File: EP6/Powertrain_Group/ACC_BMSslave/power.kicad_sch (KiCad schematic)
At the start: 11 parts, among them IC2 LT8631IFE#PBF

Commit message: ACC_BMSslave pcb priliminary layout
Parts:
- R50, R51, R52: footprint Resistor_SMD:R_0603_1608Metric -> Resistor_SMD:R_0402_1005Metric
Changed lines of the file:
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@@
 			)
 		)
-		(property "Footprint" "Resistor_SMD:R_0603_1608Metric"
+		(property "Footprint" "Resistor_SMD:R_0402_1005Metric"
 			(at 41.402 57.15 90)
 			(effects
@@
 			)
 		)
-		(property "Footprint" "Resistor_SMD:R_0603_1608Metric"
+		(property "Footprint" "Resistor_SMD:R_0402_1005Metric"
 			(at 116.332 54.61 90)
 			(effects
@@
 			)
 		)
-		(property "Footprint" "Resistor_SMD:R_0603_1608Metric"
+		(property "Footprint" "Resistor_SMD:R_0402_1005Metric"
 			(at 116.332 62.23 90)
 			(effects

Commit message: [BMSslave] snapshot
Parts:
- C15: renamed from C19; value 0.1u -> 100n
- renumbered C17 to C13, C18 to C14, C20 to C16, C21 to C17, C22 to C18, R50 to R20, R51 to R21, R52 to R22
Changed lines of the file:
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@@
 		(shape input)
 		(at 58.42 35.56 180)
-		(fields_autoplaced yes)
 		(effects
 			(font
@@
 		(shape input)
 		(at 40.64 30.48 180)
-		(fields_autoplaced yes)
 		(effects
 			(font
@@
 		(shape output)
 		(at 152.4 50.8 0)
-		(fields_autoplaced yes)
 		(effects
 			(font
@@
 		(dnp no)
 		(fields_autoplaced yes)
-		(property "Reference" "C21"
+		(property "Reference" "C17"
 			(at 138.43 41.91 0)
 			(effects
@@
 			(project "BMS_Slave_V1(ADBMS1818)"
 				(path "/0942010f-46b1-4fe9-9f5e-a3ebd22b3e41/46164ab6-bc7a-458b-aa2e-57ce2cac15f0"
-					(reference "C21")
+					(reference "C17")
 					(unit 1)
 				)
@@
 		(dnp no)
 		(fields_autoplaced yes)
-		(property "Reference" "#PWR059"
+		(property "Reference" "#PWR031"
 			(at 80.01 80.01 0)
 			(effects
@@
 			(project "BMS_Slave_V1(ADBMS1818)"
 				(path "/0942010f-46b1-4fe9-9f5e-a3ebd22b3e41/46164ab6-bc7a-458b-aa2e-57ce2cac15f0"
-					(reference "#PWR059")
+					(reference "#PWR031")
 					(unit 1)
 				)
@@
 		(dnp no)
 		(fields_autoplaced yes)
-		(property "Reference" "C17"
+		(property "Reference" "C13"
 			(at 46.99 33.02 0)
 			(effects
@@
 			(project "BMS_Slave_V1(ADBMS1818)"
 				(path "/0942010f-46b1-4fe9-9f5e-a3ebd22b3e41/46164ab6-bc7a-458b-aa2e-57ce2cac15f0"
-					(reference "C17")
+					(reference "C13")
 					(unit 1)
 				)
@@
 		(dnp no)
 		(fields_autoplaced yes)
-		(property "Reference" "#PWR062"
+		(property "Reference" "#PWR034"
 			(at 134.62 64.77 0)
 			(effects
@@
 			(project "BMS_Slave_V1(ADBMS1818)"
 				(path "/0942010f-46b1-4fe9-9f5e-a3ebd22b3e41/46164ab6-bc7a-458b-aa2e-57ce2cac15f0"
-					(reference "#PWR062")
+					(reference "#PWR034")
 					(unit 1)
 				)
@@
 		(dnp no)
 		(fields_autoplaced yes)
-		(property "Reference" "C18"
+		(property "Reference" "C14"
 			(at 57.15 55.88 0)
 			(effects
@@
 			(project "BMS_Slave_V1(ADBMS1818)"
 				(path "/0942010f-46b1-4fe9-9f5e-a3ebd22b3e41/46164ab6-bc7a-458b-aa2e-57ce2cac15f0"
-					(reference "C18")
+					(reference "C14")
 					(unit 1)
 				)
@@
 		(dnp no)
 		(fields_autoplaced yes)
-		(property "Reference" "R50"
+		(property "Reference" "R20"
 			(at 45.72 55.88 0)
 			(effects
@@
 			(project "BMS_Slave_V1(ADBMS1818)"
 				(path "/0942010f-46b1-4fe9-9f5e-a3ebd22b3e41/46164ab6-bc7a-458b-aa2e-57ce2cac15f0"
-					(reference "R50")
+					(reference "R20")
 					(unit 1)
 				)
@@
 		(dnp no)
 		(fields_autoplaced yes)
-		(property "Reference" "R51"
+		(property "Reference" "R21"
 			(at 120.65 53.34 0)
 			(effects
@@
 			(project "BMS_Slave_V1(ADBMS1818)"
 				(path "/0942010f-46b1-4fe9-9f5e-a3ebd22b3e41/46164ab6-bc7a-458b-aa2e-57ce2cac15f0"
-					(reference "R51")
+					(reference "R21")
 					(unit 1)
 				)
@@
 		(dnp no)
 		(fields_autoplaced yes)
-		(property "Reference" "#PWR060"
+		(property "Reference" "#PWR032"
 			(at 118.11 72.39 0)
 			(effects
@@
 			(project "BMS_Slave_V1(ADBMS1818)"
 				(path "/0942010f-46b1-4fe9-9f5e-a3ebd22b3e41/46164ab6-bc7a-458b-aa2e-57ce2cac15f0"
-					(reference "#PWR060")
+					(reference "#PWR032")
 					(unit 1)
 				)
@@
 		(dnp no)
 		(fields_autoplaced yes)
-		(property "Reference" "C22"
+		(property "Reference" "C18"
 			(at 138.43 53.34 0)
 			(effects
@@
 			(project "BMS_Slave_V1(ADBMS1818)"
 				(path "/0942010f-46b1-4fe9-9f5e-a3ebd22b3e41/46164ab6-bc7a-458b-aa2e-57ce2cac15f0"
-					(reference "C22")
+					(reference "C18")
 					(unit 1)
 				)
@@
 		(dnp no)
 		(fields_autoplaced yes)
-		(property "Reference" "#PWR058"
+		(property "Reference" "#PWR030"
 			(at 43.18 44.45 0)
 			(effects
@@
 			(project "BMS_Slave_V1(ADBMS1818)"
 				(path "/0942010f-46b1-4fe9-9f5e-a3ebd22b3e41/46164ab6-bc7a-458b-aa2e-57ce2cac15f0"
-					(reference "#PWR058")
+					(reference "#PWR030")
 					(unit 1)
 				)
@@
 		(dnp no)
 		(fields_autoplaced yes)
-		(property "Reference" "C19"
+		(property "Reference" "C15"
 			(at 104.14 27.94 90)
 			(effects
@@
 			)
 		)
-		(property "Value" "0.1u"
+		(property "Value" "100n"
 			(at 104.14 30.48 90)
 			(effects
@@
 			(project "BMS_Slave_V1(ADBMS1818)"
 				(path "/0942010f-46b1-4fe9-9f5e-a3ebd22b3e41/46164ab6-bc7a-458b-aa2e-57ce2cac15f0"
-					(reference "C19")
+					(reference "C15")
 					(unit 1)
 				)
@@
 		(dnp no)
 		(fields_autoplaced yes)
-		(property "Reference" "#PWR061"
+		(property "Reference" "#PWR033"
 			(at 134.62 53.34 0)
 			(effects
@@
 			(project "BMS_Slave_V1(ADBMS1818)"
 				(path "/0942010f-46b1-4fe9-9f5e-a3ebd22b3e41/46164ab6-bc7a-458b-aa2e-57ce2cac15f0"
-					(reference "#PWR061")
+					(reference "#PWR033")
 					(unit 1)
 				)
@@
 		(dnp no)
 		(fields_autoplaced yes)
-		(property "Reference" "R52"
+		(property "Reference" "R22"
 			(at 120.65 60.96 0)
 			(effects
@@
 			(project "BMS_Slave_V1(ADBMS1818)"
 				(path "/0942010f-46b1-4fe9-9f5e-a3ebd22b3e41/46164ab6-bc7a-458b-aa2e-57ce2cac15f0"
-					(reference "R52")
+					(reference "R22")
 					(unit 1)
 				)
@@
 		(dnp no)
 		(fields_autoplaced yes)
-		(property "Reference" "C20"
+		(property "Reference" "C16"
 			(at 107.95 53.34 0)
 			(effects
@@
 			(project "BMS_Slave_V1(ADBMS1818)"
 				(path "/0942010f-46b1-4fe9-9f5e-a3ebd22b3e41/46164ab6-bc7a-458b-aa2e-57ce2cac15f0"
-					(reference "C20")
-					(unit 1)
-				)
+					(reference "C16")
+					(unit 1)
+				)

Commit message: [BMSslave] snapshot
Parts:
- renumbered R20 to R17, R21 to R18, R22 to R19
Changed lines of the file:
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@@
 (kicad_sch
-	(version 20231120)
+	(version 20250114)
 	(generator "eeschema")
-	(generator_version "8.0")
+	(generator_version "9.0")
 	(paper "A4")
 	(junction
@@
 		(shape input)
 		(at 58.42 35.56 180)
-		(fields_autoplaced yes)
 		(effects
 			(font
@@
 		(shape input)
 		(at 40.64 30.48 180)
-		(fields_autoplaced yes)
 		(effects
 			(font
@@
 		(shape output)
 		(at 152.4 50.8 0)
-		(fields_autoplaced yes)
 		(effects
 			(font
@@
 		(dnp no)
 		(fields_autoplaced yes)
-		(property "Reference" "#PWR031"
+		(property "Reference" "#PWR054"
 			(at 80.01 80.01 0)
 			(effects
@@
 			(project "BMS_Slave_V1(ADBMS1818)"
 				(path "/0942010f-46b1-4fe9-9f5e-a3ebd22b3e41/46164ab6-bc7a-458b-aa2e-57ce2cac15f0"
-					(reference "#PWR031")
+					(reference "#PWR054")
 					(unit 1)
 				)
@@
 		(dnp no)
 		(fields_autoplaced yes)
-		(property "Reference" "#PWR034"
+		(property "Reference" "#PWR057"
 			(at 134.62 64.77 0)
 			(effects
@@
 			(project "BMS_Slave_V1(ADBMS1818)"
 				(path "/0942010f-46b1-4fe9-9f5e-a3ebd22b3e41/46164ab6-bc7a-458b-aa2e-57ce2cac15f0"
-					(reference "#PWR034")
+					(reference "#PWR057")
 					(unit 1)
 				)
@@
 		(dnp no)
 		(fields_autoplaced yes)
-		(property "Reference" "R20"
+		(property "Reference" "R17"
 			(at 45.72 55.88 0)
 			(effects
@@
 			(project "BMS_Slave_V1(ADBMS1818)"
 				(path "/0942010f-46b1-4fe9-9f5e-a3ebd22b3e41/46164ab6-bc7a-458b-aa2e-57ce2cac15f0"
-					(reference "R20")
+					(reference "R17")
 					(unit 1)
 				)
@@
 		(dnp no)
 		(fields_autoplaced yes)
-		(property "Reference" "R21"
+		(property "Reference" "R18"
 			(at 120.65 53.34 0)
 			(effects
@@
 			(project "BMS_Slave_V1(ADBMS1818)"
 				(path "/0942010f-46b1-4fe9-9f5e-a3ebd22b3e41/46164ab6-bc7a-458b-aa2e-57ce2cac15f0"
-					(reference "R21")
+					(reference "R18")
 					(unit 1)
 				)
@@
 		(dnp no)
 		(fields_autoplaced yes)
-		(property "Reference" "#PWR032"
+		(property "Reference" "#PWR055"
 			(at 118.11 72.39 0)
 			(effects
@@
 			(project "BMS_Slave_V1(ADBMS1818)"
 				(path "/0942010f-46b1-4fe9-9f5e-a3ebd22b3e41/46164ab6-bc7a-458b-aa2e-57ce2cac15f0"
-					(reference "#PWR032")
+					(reference "#PWR055")
 					(unit 1)
 				)
@@
 		(dnp no)
 		(fields_autoplaced yes)
-		(property "Reference" "#PWR030"
+		(property "Reference" "#PWR053"
 			(at 43.18 44.45 0)
 			(effects
@@
 			(project "BMS_Slave_V1(ADBMS1818)"
 				(path "/0942010f-46b1-4fe9-9f5e-a3ebd22b3e41/46164ab6-bc7a-458b-aa2e-57ce2cac15f0"
-					(reference "#PWR030")
+					(reference "#PWR053")
 					(unit 1)
 				)
@@
 		(dnp no)
 		(fields_autoplaced yes)
-		(property "Reference" "#PWR033"
+		(property "Reference" "#PWR056"
 			(at 134.62 53.34 0)
 			(effects
@@
 			(project "BMS_Slave_V1(ADBMS1818)"
 				(path "/0942010f-46b1-4fe9-9f5e-a3ebd22b3e41/46164ab6-bc7a-458b-aa2e-57ce2cac15f0"
-					(reference "#PWR033")
+					(reference "#PWR056")
 					(unit 1)
 				)
@@
 		(dnp no)
 		(fields_autoplaced yes)
-		(property "Reference" "R22"
+		(property "Reference" "R19"
 			(at 120.65 60.96 0)
 			(effects
@@
 			(project "BMS_Slave_V1(ADBMS1818)"
 				(path "/0942010f-46b1-4fe9-9f5e-a3ebd22b3e41/46164ab6-bc7a-458b-aa2e-57ce2cac15f0"
-					(reference "R22")
-					(unit 1)
-				)
+					(reference "R19")
+					(unit 1)
+				)

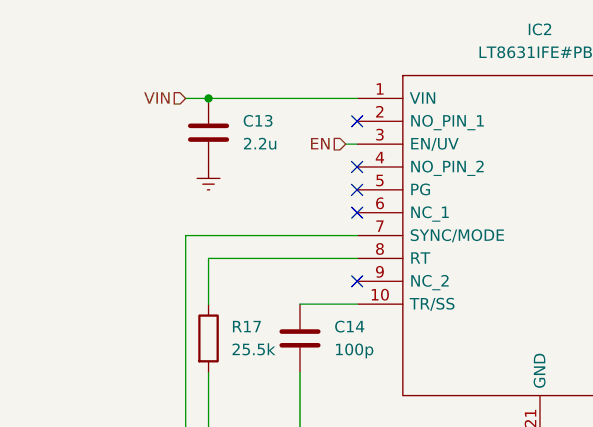
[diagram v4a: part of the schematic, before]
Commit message: [BMSslave] update layout
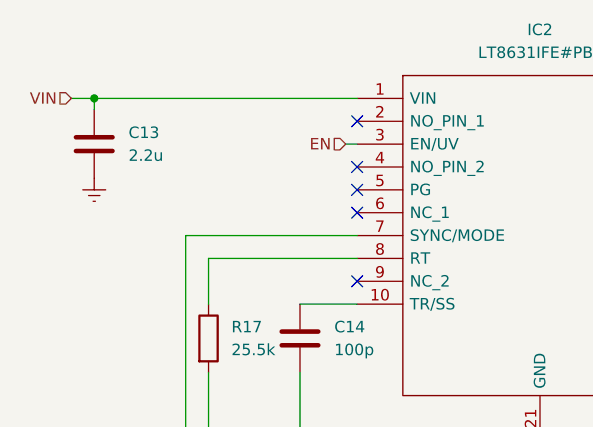
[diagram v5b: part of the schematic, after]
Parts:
- C16: footprint Capacitor_SMD:C_0603_1608Metric -> Capacitor_SMD:C_0402_1005Metric
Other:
- moved on the sheet: C13
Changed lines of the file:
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@@
 	)
 	(junction
-		(at 43.18 30.48)
+		(at 30.48 30.48)
 		(diameter 0)
 		(color 0 0 0 0)
@@
 	(wire
 		(pts
-			(xy 40.64 30.48) (xy 43.18 30.48)
+			(xy 27.94 30.48) (xy 30.48 30.48)
 		)
 		(stroke
@@
 	(wire
 		(pts
-			(xy 43.18 30.48) (xy 59.69 30.48)
+			(xy 30.48 30.48) (xy 59.69 30.48)
 		)
 		(stroke
@@
 		(pts
 			(xy 118.11 35.56) (xy 118.11 45.72)
+		)
+		(stroke
+			(width 0)
+			(type default)
+		)
+	)
+	(wire
+		(pts
+			(xy 30.48 31.75) (xy 30.48 30.48)
 		)
 		(stroke
@@
 	(hierarchical_label "VIN"
 		(shape input)
-		(at 40.64 30.48 180)
+		(at 27.94 30.48 180)
 		(effects
 			(font
@@
 	(symbol
 		(lib_id "Device:C")
-		(at 43.18 34.29 0)
+		(at 30.48 35.56 0)
 		(unit 1)
 		(exclude_from_sim no)
@@
 		(fields_autoplaced yes)
 		(property "Reference" "C13"
-			(at 46.99 33.02 0)
+			(at 34.29 34.29 0)
 			(effects
 				(font
@@
 		)
 		(property "Value" "2.2u"
-			(at 46.99 35.56 0)
+			(at 34.29 36.83 0)
 			(effects
 				(font
@@
 		)
 		(property "Footprint" "Capacitor_SMD:C_2220_5750Metric"
-			(at 44.1452 38.1 0)
+			(at 31.4452 39.37 0)
 			(effects
 				(font
@@
 		)
 		(property "Datasheet" "~"
-			(at 43.18 34.29 0)
+			(at 30.48 35.56 0)
 			(effects
 				(font
@@
 		)
 		(property "Description" ""
-			(at 43.18 34.29 0)
+			(at 30.48 35.56 0)
 			(effects
 				(font
@@
 		(on_board yes)
 		(dnp no)
-		(fields_autoplaced yes)
 		(property "Reference" "R17"
 			(at 45.72 55.88 0)
@@
 	(symbol
 		(lib_id "power:Earth")
-		(at 43.18 38.1 0)
+		(at 30.48 39.37 0)
 		(unit 1)
 		(exclude_from_sim no)
@@
 		(fields_autoplaced yes)
 		(property "Reference" "#PWR053"
-			(at 43.18 44.45 0)
+			(at 30.48 45.72 0)
 			(effects
 				(font
@@
 		)
 		(property "Value" "Earth"
-			(at 43.18 41.91 0)
+			(at 30.48 43.18 0)
 			(effects
 				(font
@@
 		)
 		(property "Footprint" ""
-			(at 43.18 38.1 0)
+			(at 30.48 39.37 0)
 			(effects
 				(font
@@
 		)
 		(property "Datasheet" "~"
-			(at 43.18 38.1 0)
+			(at 30.48 39.37 0)
 			(effects
 				(font
@@
 		)
 		(property "Description" ""
-			(at 43.18 38.1 0)
+			(at 30.48 39.37 0)
 			(effects
 				(font
@@
 			)
 		)
-		(property "Footprint" "Capacitor_SMD:C_0603_1608Metric"
+		(property "Footprint" "Capacitor_SMD:C_0402_1005Metric"
 			(at 103.1748 50.8 0)
 			(effects

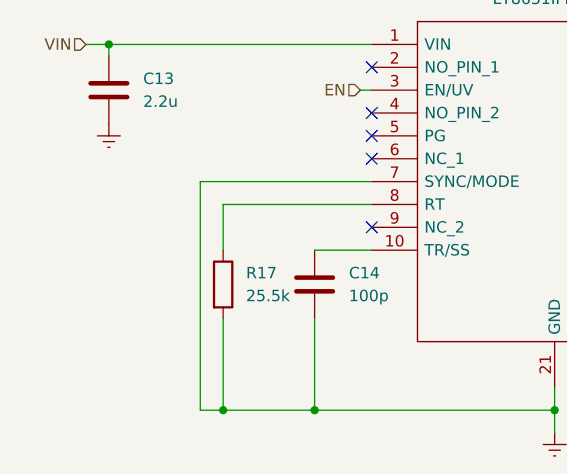
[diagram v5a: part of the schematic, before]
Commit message: update ACC_BMSslave to V3.1
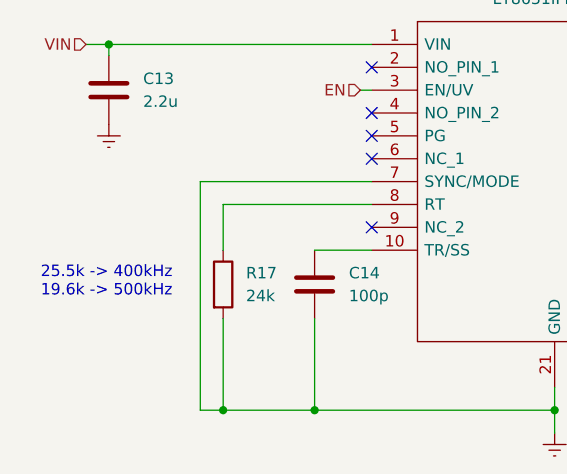
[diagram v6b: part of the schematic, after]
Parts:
- R17: value 25.5k -> 24k
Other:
- note added: "25.5k -> 400kHz 19.6k -> 500kHz"
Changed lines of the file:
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@@
 	(generator_version "9.0")
 	(paper "A4")
+	(text "25.5k -> 400kHz\n19.6k -> 500kHz"
+		(exclude_from_sim no)
+		(at 30.226 56.896 0)
+		(effects
+			(font
+				(size 1.27 1.27)
+			)
+		)
+	)
 	(junction
 		(at 104.14 58.42)
@@
 			)
 		)
-		(property "Value" "25.5k"
+		(property "Value" "24k"
 			(at 45.72 58.42 0)
 			(effects
